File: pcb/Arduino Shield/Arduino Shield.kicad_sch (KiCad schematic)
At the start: 40 parts, among them J1 Power, J10 CH_02, J11 CH_03, J12 CH_04, J13 CH_05, J14 Main Controller, J15 DRV_03, J16 DRV_02, J17 DRV_01, J18 EXT VCC, J19 DRV_03_PWR, J2 PWM, J20 SD_SPI, J21 DRV_02_PWR, J22 DRV_01_PWR, J23 Panel Power SW, J3 Analog, J4 PWM, J5 Analog, J6 Communication, J7 Digital, J8 SCR_SPI, J9 CH_01

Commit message: Update pcb, start channel
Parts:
- F1: footprint Fuse:Fuseholder_Cylinder-5x20mm_Stelvio-Kontek_PTF78_Horizontal_Open -> Fuse:Fuseholder_Clip-5x20mm_Eaton_1A5601-01_Inline_P20.80x6.76mm_D1.70mm_Horizontal
- J23: footprint (none) -> Connector_PinSocket_2.00mm:PinSocket_1x02_P2.00mm_Vertical
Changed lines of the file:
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@@
 		)
 	)
+	(global_label "E_VCC"
+		(shape input)
+		(at 27.94 179.07 90)
+		(fields_autoplaced yes)
+		(effects
+			(font
+				(size 1.27 1.27)
+			)
+			(justify left)
+		)
+		(property "Intersheetrefs" "${INTERSHEET_REFS}"
+			(at 27.94 170.2445 90)
+			(effects
+				(font
+					(size 1.27 1.27)
+				)
+				(justify left)
+				(hide yes)
+			)
+		)
+	)
 	(global_label "CH3_FADER_OUT"
 		(shape input)
@@
 		)
 	)
-	(global_label "GND"
-		(shape output)
-		(at 68.58 187.96 270)
-		(fields_autoplaced yes)
-		(effects
-			(font
-				(size 1.27 1.27)
-			)
-			(justify right)
-		)
-		(property "Intersheetrefs" "${INTERSHEET_REFS}"
-			(at 68.58 194.9108 90)
-			(effects
-				(font
-					(size 1.27 1.27)
-				)
-				(justify right)
-				(hide yes)
-			)
-		)
-	)
-	(global_label "E_VCC"
-		(shape output)
-		(at 27.94 179.07 90)
-		(fields_autoplaced yes)
-		(effects
-			(font
-				(size 1.27 1.27)
-			)
-			(justify left)
-		)
-		(property "Intersheetrefs" "${INTERSHEET_REFS}"
-			(at 27.94 170.2445 90)
-			(effects
-				(font
-					(size 1.27 1.27)
-				)
-				(justify left)
-				(hide yes)
-			)
-		)
-	)
 	(global_label "CH5_ENC_DT"
 		(shape input)
@@
 		)
 	)
+	(global_label "GND"
+		(shape input)
+		(at 68.58 187.96 270)
+		(fields_autoplaced yes)
+		(effects
+			(font
+				(size 1.27 1.27)
+			)
+			(justify right)
+		)
+		(property "Intersheetrefs" "${INTERSHEET_REFS}"
+			(at 68.58 194.9108 90)
+			(effects
+				(font
+					(size 1.27 1.27)
+				)
+				(justify right)
+				(hide yes)
+			)
+		)
+	)
 	(global_label "E_VCC"
 		(shape input)
@@
 			)
 		)
-		(property "Footprint" "Fuse:Fuseholder_Cylinder-5x20mm_Stelvio-Kontek_PTF78_Horizontal_Open"
+		(property "Footprint" "Fuse:Fuseholder_Clip-5x20mm_Eaton_1A5601-01_Inline_P20.80x6.76mm_D1.70mm_Horizontal"
 			(at 63.5 183.388 90)
 			(effects
@@
 			)
 		)
-		(property "Footprint" ""
+		(property "Footprint" "Connector_PinSocket_2.00mm:PinSocket_1x02_P2.00mm_Vertical"
 			(at 91.44 185.42 0)
 			(effects

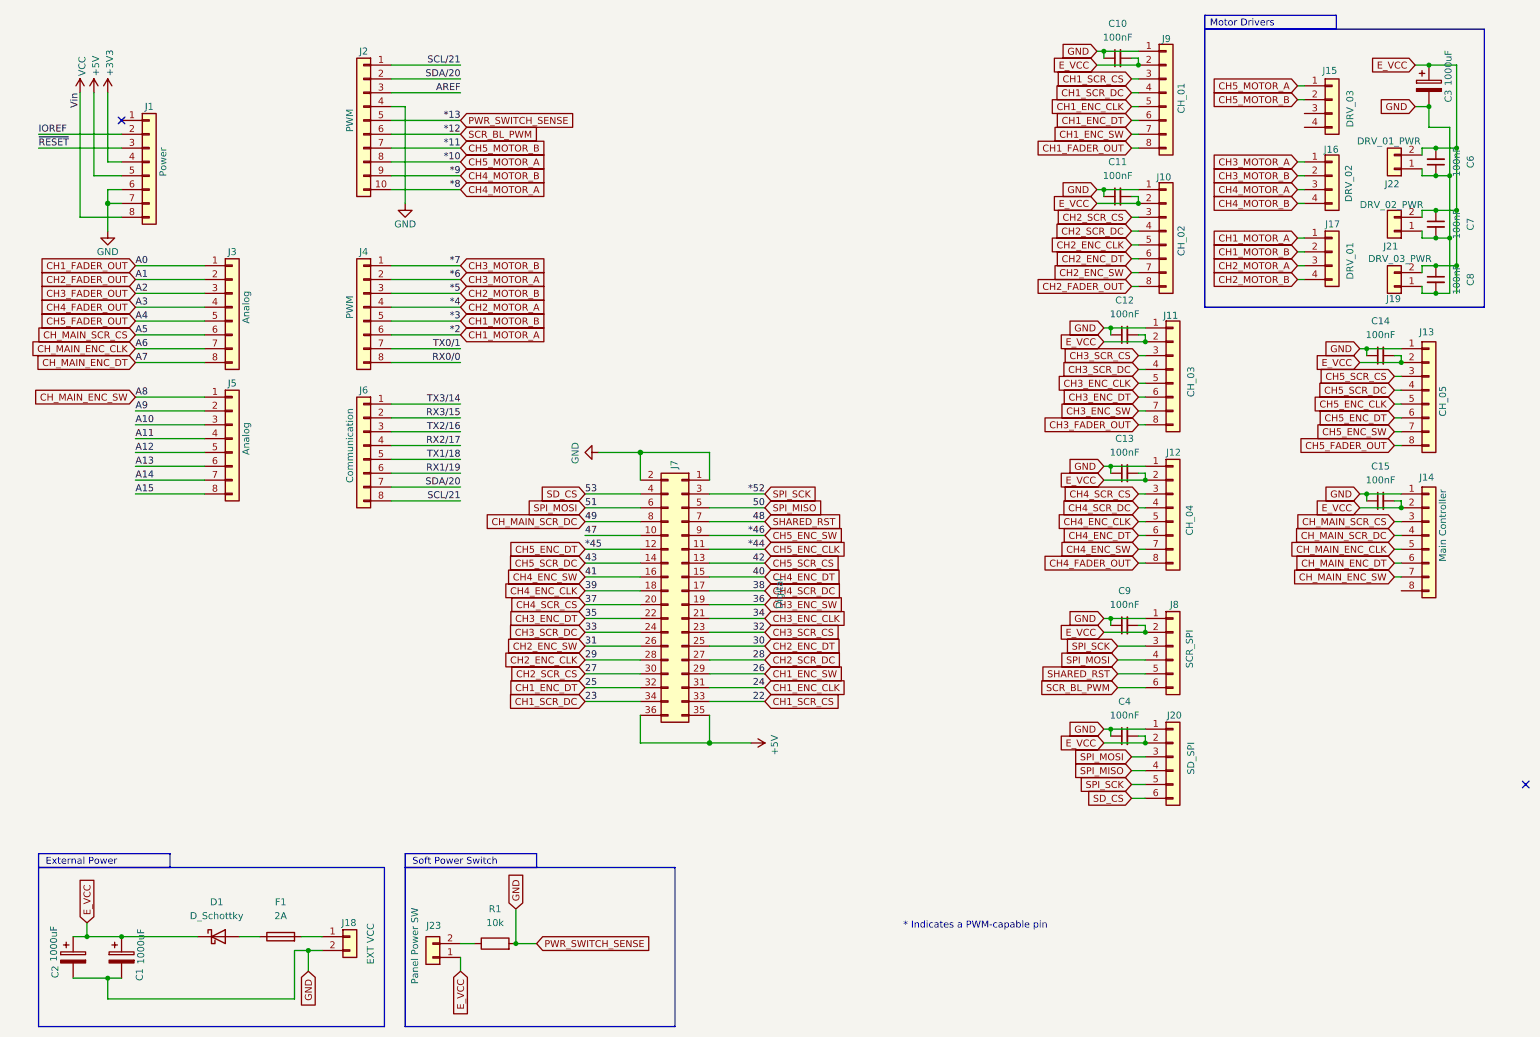
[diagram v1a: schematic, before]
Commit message: Update main PCB to use 9pin connectors for channels (They need unique RST)
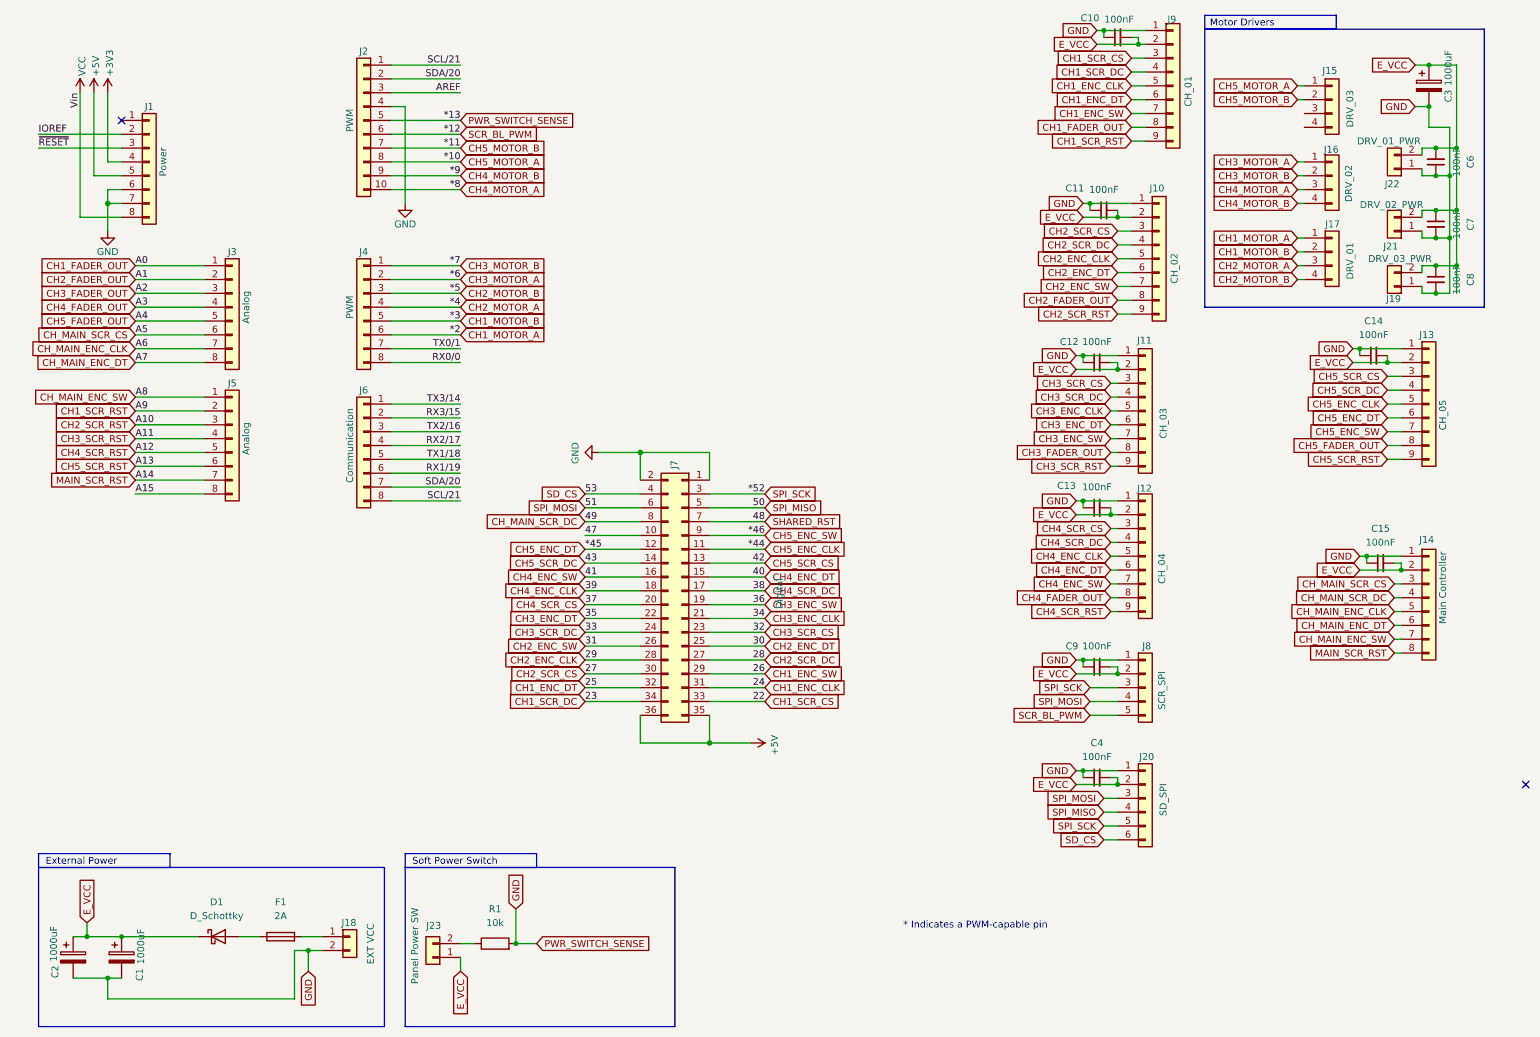
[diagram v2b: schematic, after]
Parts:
- J10, J11, J12, J13, J9: footprint Connector_PinSocket_2.00mm:PinSocket_1x08_P2.00mm_Vertical -> Connector_PinSocket_2.00mm:PinSocket_1x09_P2.00mm_Vertical; symbol Connector_Generic:Conn_01x08 -> Connector_Generic:Conn_01x09
- J8: footprint Connector_PinSocket_2.00mm:PinSocket_1x06_P2.00mm_Vertical -> Connector_PinSocket_2.00mm:PinSocket_1x05_P2.00mm_Vertical; symbol Connector_Generic:Conn_01x06 -> Connector_Generic:Conn_01x05
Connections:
- net A14 is gone; now on net MAIN_SCR_RST: J5.7 (Pin_7)
- net SCR_BL_PWM: now also J8.5 (Pin_5); no longer J8.6 (Pin_6)
- net SHARED_RST: no longer J8.5 (Pin_5)
- net MAIN_SCR_RST: now reaches J14.8 (Pin_8)
- net A10 renamed CH2_SCR_RST
- net CH2_SCR_RST: now also J10.9 (Pin_9)
- net A11 renamed CH3_SCR_RST
- net CH3_SCR_RST: now also J11.9 (Pin_9)
- net A12 renamed CH4_SCR_RST
- net CH4_SCR_RST: now also J12.9 (Pin_9)
- net A13 renamed CH5_SCR_RST
- net CH5_SCR_RST: now also J13.9 (Pin_9)
- net A9 renamed CH1_SCR_RST
- net CH1_SCR_RST: now also J9.9 (Pin_9)
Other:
- moved on the sheet: C10, C11, C12, C13, C14, C15, C4, C9, J14, J20
